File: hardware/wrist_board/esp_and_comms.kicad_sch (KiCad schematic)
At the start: 0 parts

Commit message: Added flex sensor circuitry and ESP
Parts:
- added C5, C6, C7, C8, C9: 0.1uF, symbol Device:C_Small_US
- added R10, R11, R7, R8, R9: 22k, symbol Device:R_Small
- added R6: 10k, symbol Device:R_Small
- added X1: ESP32-S3-WROOM-1-N16R8, ESP32-S3-WROOM-1-N16R8:ESP32S3WROOM1N8R2, symbol ESP32-S3-WROOM-1-N16R8:ESP32-S3-WROOM-1-N16R8
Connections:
- new net: R6.2, X1.3 (EN)
- new net +3V3: R10.2, R11.2, R6.1, R7.2, R8.2, R9.2, X1.2 (3V3)
- new net D+: X1.14 (IO20)
- new net D-: X1.13 (IO19)
- new net FS_1: C5.1, R7.1, X1.4 (IO4)
- new net FS_2: C6.1, R8.1, X1.5 (IO5)
- new net FS_3: C7.1, R9.1, X1.6 (IO6)
- new net FS_4: C8.1, R10.1, X1.7 (IO7)
- new net FS_5: C9.1, R11.1, X1.12 (IO8)
- new net GND: C5.2, C6.2, C7.2, C8.2, C9.2, X1.1 (GND), X1.40 (GND), X1.41 (GND), X1.42 (GND), X1.43 (GND), X1.44 (GND), X1.45 (GND), X1.46 (GND), X1.47 (GND), X1.48 (GND), X1.49 (GND)

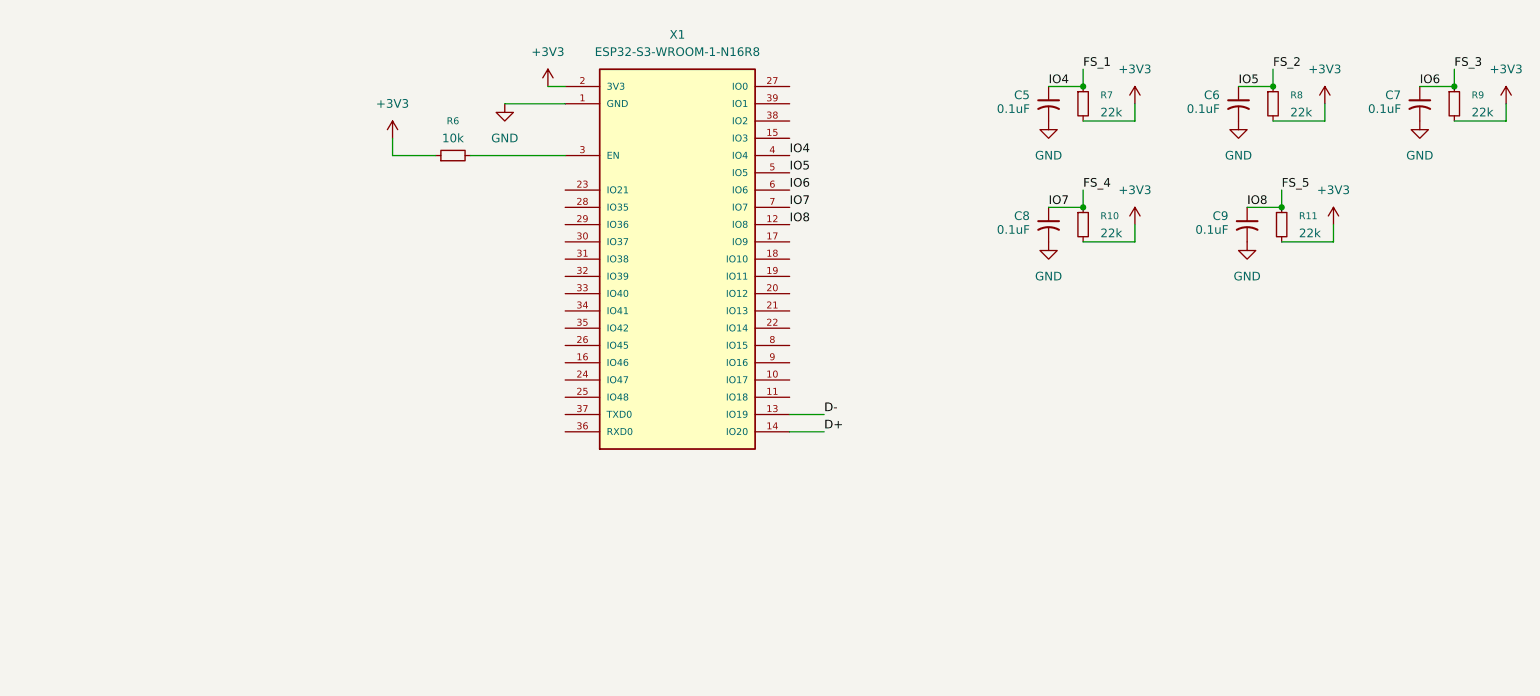
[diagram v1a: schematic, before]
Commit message: MPU 6050 IMU circuitry added
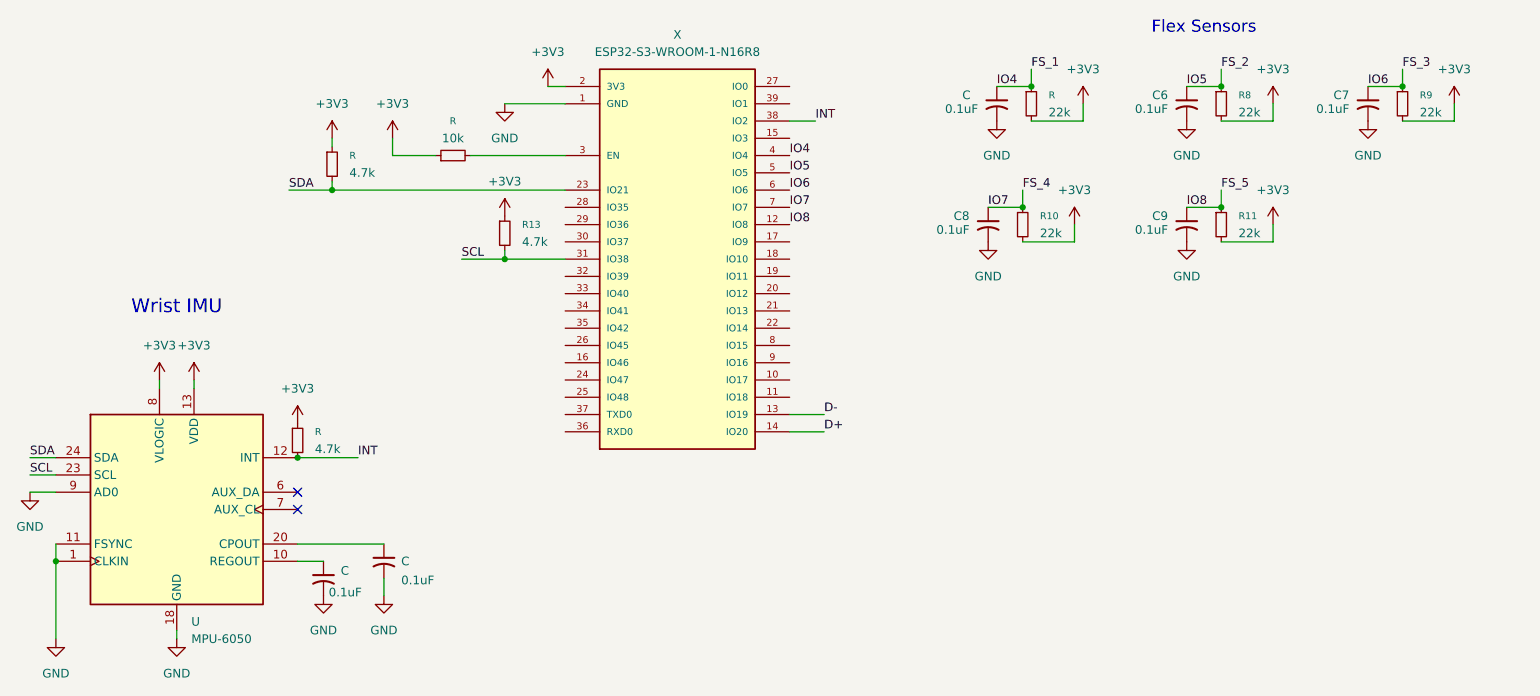
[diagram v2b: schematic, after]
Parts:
- added C (x2): 0.1uF, symbol Device:C_Small_US
- added R (x2), R13: 4.7k, symbol Device:R_Small
- added U: MPU-6050, Sensor_Motion:InvenSense_QFN-24_4x4mm_P0.5mm, symbol Sensor_Motion:MPU-6050
- renumbered C5 to C, R7 to R, R6 to R, X1 to X
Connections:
- net +3V3: now also R.1, R.1, R13.1, U.13 (VDD), U.8 (VLOGIC)
- net GND: now also C.2, C.2, U.1 (CLKIN), U.11 (FSYNC), U.18 (GND), U.9 (AD0)
- net SDA: now reaches X.23 (IO21)
- net SDA: now also R.2, U.24 (SDA)
- net SCL: now reaches X.31 (IO38)
- net SCL: now also R13.2, U.23 (SCL)
- net INT: now reaches X.38 (IO2)
- net INT: now also R.2, U.12 (INT)
- new net: C.1, U.10 (REGOUT)
- new net: C.1, U.20 (CPOUT)
- no-connect marks 0 -> 2
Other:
- note added: "Flex Sensors"
- note added: "Wrist IMU"
- moved on the sheet: C, C6, C7, C8, C9, R, R10, R11, R8, R9

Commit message: Added LEDs and power switch to power schematic
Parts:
- renumbered C to C10, C to C11, C to C5, R to R12, R to R14, R to R6, R to R7, U to U3, X to X1
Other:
- note removed: "Wrist IMU"
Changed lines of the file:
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@@
 		)
 	)
-	(text "Wrist IMU\n"
-		(exclude_from_sim no)
-		(at 69.85 108.712 0)
-		(effects
-			(font
-				(size 2.032 2.032)
-			)
-		)
-	)
 	(junction
 		(at 223.52 76.2)
@@
 		(on_board yes)
 		(dnp no)
-		(property "Reference" "C"
+		(property "Reference" "C5"
 			(at 185.42 77.47 0)
 			(effects
@@
 		(pin "1"
 		)
-		(instances)
 	)
 	(symbol
@@
 		(dnp no)
 		(fields_autoplaced yes)
-		(property "Reference" "X"
+		(property "Reference" "X1"
 			(at 143.51 68.58 0)
 			(effects
@@
 		(pin "14"
 		)
-		(instances)
 	)
 	(symbol
@@
 		(dnp no)
 		(fields_autoplaced yes)
-		(property "Reference" "U"
+		(property "Reference" "U3"
 			(at 71.9933 154.94 0)
 			(effects
@@
 		(pin "10"
 		)
-		(instances)
 	)
 	(symbol
@@
 		(dnp no)
 		(fields_autoplaced yes)
-		(property "Reference" "#PWR"
+		(property "Reference" "#PWR031"
 			(at 92.71 87.63 0)
 			(effects
@@
 		(pin "1"
 		)
-		(instances)
 	)
 	(symbol
@@
 		(dnp no)
 		(fields_autoplaced yes)
-		(property "Reference" "R"
+		(property "Reference" "R7"
 			(at 198.12 77.4699 0)
 			(effects
@@
 		(pin "1"
 		)
-		(instances)
 	)
 	(symbol
@@
 		(dnp no)
 		(fields_autoplaced yes)
-		(property "Reference" "R"
+		(property "Reference" "R14"
 			(at 90.17 126.9999 0)
 			(effects
@@
 		(pin "1"
 		)
-		(instances)
 	)
 	(symbol
@@
 		(on_board yes)
 		(dnp no)
-		(property "Reference" "C"
+		(property "Reference" "C11"
 			(at 102.87 146.05 0)
 			(effects
@@
 		(pin "1"
 		)
-		(instances)
 	)
 	(symbol
@@
 		(dnp no)
 		(fields_autoplaced yes)
-		(property "Reference" "#PWR"
+		(property "Reference" "#PWR016"
 			(at 203.2 82.55 0)
 			(effects
@@
 		(pin "1"
 		)
-		(instances)
 	)
 	(symbol
@@
 		(dnp no)
 		(fields_autoplaced yes)
-		(property "Reference" "R"
+		(property "Reference" "R6"
 			(at 110.49 81.28 90)
 			(effects
@@
 		(pin "2"
 		)
-		(instances)
 	)
 	(symbol
@@
 		(dnp no)
 		(fields_autoplaced yes)
-		(property "Reference" "#PWR"
+		(property "Reference" "#PWR013"
 			(at 124.46 80.01 0)
 			(effects
@@
 		(pin "1"
 		)
-		(instances)
 	)
 	(symbol
@@
 		(dnp no)
 		(fields_autoplaced yes)
-		(property "Reference" "#PWR"
+		(property "Reference" "#PWR028"
 			(at 69.85 163.83 0)
 			(effects
@@
 		(pin "1"
 		)
-		(instances)
 	)
 	(symbol
@@
 		(dnp no)
 		(fields_autoplaced yes)
-		(property "Reference" "#PWR"
+		(property "Reference" "#PWR034"
 			(at 87.63 129.54 0)
 			(effects
@@
 		(pin "1"
 		)
-		(instances)
 	)
 	(symbol
@@
 		(dnp no)
 		(fields_autoplaced yes)
-		(property "Reference" "R"
+		(property "Reference" "R12"
 			(at 95.25 86.3599 0)
 			(effects
@@
 		(pin "1"
 		)
-		(instances)
 	)
 	(symbol
@@
 		(dnp no)
 		(fields_autoplaced yes)
-		(property "Reference" "#PWR"
+		(property "Reference" "#PWR033"
 			(at 48.26 142.24 0)
 			(effects
@@
 		(pin "1"
 		)
-		(instances)
 	)
 	(symbol
@@
 		(dnp no)
 		(fields_autoplaced yes)
-		(property "Reference" "#PWR"
+		(property "Reference" "#PWR014"
 			(at 118.11 85.09 0)
 			(effects
@@
 		(pin "1"
 		)
-		(instances)
 	)
 	(symbol
@@
 		(dnp no)
 		(fields_autoplaced yes)
-		(property "Reference" "#PWR"
+		(property "Reference" "#PWR027"
 			(at 67.31 123.19 0)
 			(effects
@@
 		(pin "1"
 		)
-		(instances)
 	)
 	(symbol
@@
 		(dnp no)
 		(fields_autoplaced yes)
-		(property "Reference" "#PWR"
+		(property "Reference" "#PWR030"
 			(at 100.33 157.48 0)
 			(effects
@@
 		(pin "1"
 		)
-		(instances)
 	)
 	(symbol
@@
 		(dnp no)
 		(fields_autoplaced yes)
-		(property "Reference" "#PWR"
+		(property "Reference" "#PWR029"
 			(at 91.44 157.48 0)
 			(effects
@@
 		(pin "1"
 		)
-		(instances)
 	)
 	(symbol
@@
 		(dnp no)
 		(fields_autoplaced yes)
-		(property "Reference" "#PWR"
+		(property "Reference" "#PWR015"
 			(at 101.6 87.63 0)
 			(effects
@@
 		(pin "1"
 		)
-		(instances)
 	)
 	(symbol
@@
 		(dnp no)
 		(fields_autoplaced yes)
-		(property "Reference" "#PWR"
+		(property "Reference" "#PWR026"
 			(at 72.39 123.19 0)
 			(effects
@@
 		(pin "1"
 		)
-		(instances)
 	)
 	(symbol
@@
 		(dnp no)
 		(fields_autoplaced yes)
-		(property "Reference" "#PWR"
+		(property "Reference" "#PWR017"
 			(at 190.5 87.63 0)
 			(effects
@@
 		(pin "1"
 		)
-		(instances)
 	)
 	(symbol
@@
 		(on_board yes)
 		(dnp no)
-		(property "Reference" "C"
+		(property "Reference" "C10"
 			(at 93.98 147.4469 0)
 			(effects
@@
 		(pin "1"
 		)
-		(instances)
 	)
 	(symbol

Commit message: USB C 2.0 receptacle updated
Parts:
- renumbered C5 to C?, C11 to C?, C10 to C?, R7 to R?, R14 to R?, R6 to R?, R12 to R?, U3 to U?, X1 to X?
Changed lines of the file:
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@@
 		(on_board yes)
 		(dnp no)
-		(property "Reference" "C5"
+		(property "Reference" "C?"
 			(at 185.42 77.47 0)
 			(effects
@@
 		(pin "1"
 		)
+		(instances
+			(project "wrist_board"
+				(path "/530b8e3e-eee5-4922-ab86-607fb3fa4192/d316cad0-6949-4839-9637-d12d2d6e31b9"
+					(reference "C?")
+					(unit 1)
+				)
+			)
+		)
 	)
 	(symbol
@@
 		(dnp no)
 		(fields_autoplaced yes)
-		(property "Reference" "X1"
+		(property "Reference" "X?"
 			(at 143.51 68.58 0)
 			(effects
@@
 		(pin "14"
 		)
+		(instances
+			(project "wrist_board"
+				(path "/530b8e3e-eee5-4922-ab86-607fb3fa4192/d316cad0-6949-4839-9637-d12d2d6e31b9"
+					(reference "X?")
+					(unit 1)
+				)
+			)
+		)
 	)
 	(symbol
@@
 		(dnp no)
 		(fields_autoplaced yes)
-		(property "Reference" "U3"
+		(property "Reference" "U?"
 			(at 71.9933 154.94 0)
 			(effects
@@
 		(pin "10"
 		)
+		(instances
+			(project "wrist_board"
+				(path "/530b8e3e-eee5-4922-ab86-607fb3fa4192/d316cad0-6949-4839-9637-d12d2d6e31b9"
+					(reference "U?")
+					(unit 1)
+				)
+			)
+		)
 	)
 	(symbol
@@
 		(dnp no)
 		(fields_autoplaced yes)
-		(property "Reference" "#PWR031"
+		(property "Reference" "#PWR?"
 			(at 92.71 87.63 0)
 			(effects
@@
 		(pin "1"
 		)
+		(instances
+			(project "wrist_board"
+				(path "/530b8e3e-eee5-4922-ab86-607fb3fa4192/d316cad0-6949-4839-9637-d12d2d6e31b9"
+					(reference "#PWR?")
+					(unit 1)
+				)
+			)
+		)
 	)
 	(symbol
@@
 		(dnp no)
 		(fields_autoplaced yes)
-		(property "Reference" "R7"
+		(property "Reference" "R?"
 			(at 198.12 77.4699 0)
 			(effects
@@
 		(pin "1"
 		)
+		(instances
+			(project "wrist_board"
+				(path "/530b8e3e-eee5-4922-ab86-607fb3fa4192/d316cad0-6949-4839-9637-d12d2d6e31b9"
+					(reference "R?")
+					(unit 1)
+				)
+			)
+		)
 	)
 	(symbol
@@
 		(dnp no)
 		(fields_autoplaced yes)
-		(property "Reference" "R14"
+		(property "Reference" "R?"
 			(at 90.17 126.9999 0)
 			(effects
@@
 		(pin "1"
 		)
+		(instances
+			(project "wrist_board"
+				(path "/530b8e3e-eee5-4922-ab86-607fb3fa4192/d316cad0-6949-4839-9637-d12d2d6e31b9"
+					(reference "R?")
+					(unit 1)
+				)
+			)
+		)
 	)
 	(symbol
@@
 		(on_board yes)
 		(dnp no)
-		(property "Reference" "C11"
+		(property "Reference" "C?"
 			(at 102.87 146.05 0)
 			(effects
@@
 		(pin "1"
 		)
+		(instances
+			(project "wrist_board"
+				(path "/530b8e3e-eee5-4922-ab86-607fb3fa4192/d316cad0-6949-4839-9637-d12d2d6e31b9"
+					(reference "C?")
+					(unit 1)
+				)
+			)
+		)
 	)
 	(symbol
@@
 		(dnp no)
 		(fields_autoplaced yes)
-		(property "Reference" "#PWR016"
+		(property "Reference" "#PWR?"
 			(at 203.2 82.55 0)
 			(effects
@@
 		(pin "1"
 		)
+		(instances
+			(project "wrist_board"
+				(path "/530b8e3e-eee5-4922-ab86-607fb3fa4192/d316cad0-6949-4839-9637-d12d2d6e31b9"
+					(reference "#PWR?")
+					(unit 1)
+				)
+			)
+		)
 	)
 	(symbol
@@
 		(dnp no)
 		(fields_autoplaced yes)
-		(property "Reference" "R6"
+		(property "Reference" "R?"
 			(at 110.49 81.28 90)
 			(effects
@@
 		(pin "2"
 		)
+		(instances
+			(project "wrist_board"
+				(path "/530b8e3e-eee5-4922-ab86-607fb3fa4192/d316cad0-6949-4839-9637-d12d2d6e31b9"
+					(reference "R?")
+					(unit 1)
+				)
+			)
+		)
 	)
 	(symbol
@@
 		(dnp no)
 		(fields_autoplaced yes)
-		(property "Reference" "#PWR013"
+		(property "Reference" "#PWR?"
 			(at 124.46 80.01 0)
 			(effects
@@
 		(pin "1"
 		)
+		(instances
+			(project "wrist_board"
+				(path "/530b8e3e-eee5-4922-ab86-607fb3fa4192/d316cad0-6949-4839-9637-d12d2d6e31b9"
+					(reference "#PWR?")
+					(unit 1)
+				)
+			)
+		)
 	)
 	(symbol
@@
 		(dnp no)
 		(fields_autoplaced yes)
-		(property "Reference" "#PWR028"
+		(property "Reference" "#PWR?"
 			(at 69.85 163.83 0)
 			(effects
@@
 		(pin "1"
 		)
+		(instances
+			(project "wrist_board"
+				(path "/530b8e3e-eee5-4922-ab86-607fb3fa4192/d316cad0-6949-4839-9637-d12d2d6e31b9"
+					(reference "#PWR?")
+					(unit 1)
+				)
+			)
+		)
 	)
 	(symbol
@@
 		(dnp no)
 		(fields_autoplaced yes)
-		(property "Reference" "#PWR034"
+		(property "Reference" "#PWR?"
 			(at 87.63 129.54 0)
 			(effects
@@
 		(pin "1"
 		)
+		(instances
+			(project "wrist_board"
+				(path "/530b8e3e-eee5-4922-ab86-607fb3fa4192/d316cad0-6949-4839-9637-d12d2d6e31b9"
+					(reference "#PWR?")
+					(unit 1)
+				)
+			)
+		)
 	)
 	(symbol
@@
 		(dnp no)
 		(fields_autoplaced yes)
-		(property "Reference" "R12"
+		(property "Reference" "R?"
 			(at 95.25 86.3599 0)
 			(effects
@@
 		(pin "1"
 		)
+		(instances
+			(project "wrist_board"
+				(path "/530b8e3e-eee5-4922-ab86-607fb3fa4192/d316cad0-6949-4839-9637-d12d2d6e31b9"
+					(reference "R?")
+					(unit 1)
+				)
+			)
+		)
 	)
 	(symbol
@@
 		(dnp no)
 		(fields_autoplaced yes)
-		(property "Reference" "#PWR033"
+		(property "Reference" "#PWR?"
 			(at 48.26 142.24 0)
 			(effects
@@
 		(pin "1"
 		)
+		(instances
+			(project "wrist_board"
+				(path "/530b8e3e-eee5-4922-ab86-607fb3fa4192/d316cad0-6949-4839-9637-d12d2d6e31b9"
+					(reference "#PWR?")
+					(unit 1)
+				)
+			)
+		)
 	)
 	(symbol
@@
 		(dnp no)
 		(fields_autoplaced yes)
-		(property "Reference" "#PWR014"
+		(property "Reference" "#PWR?"
 			(at 118.11 85.09 0)
 			(effects
@@
 		(pin "1"
 		)
+		(instances
+			(project "wrist_board"
+				(path "/530b8e3e-eee5-4922-ab86-607fb3fa4192/d316cad0-6949-4839-9637-d12d2d6e31b9"
+					(reference "#PWR?")
+					(unit 1)
+				)
+			)
+		)
 	)
 	(symbol
@@
 		(dnp no)
 		(fields_autoplaced yes)
-		(property "Reference" "#PWR027"
+		(property "Reference" "#PWR?"
 			(at 67.31 123.19 0)
 			(effects
@@
 		(pin "1"
 		)
+		(instances
+			(project "wrist_board"
+				(path "/530b8e3e-eee5-4922-ab86-607fb3fa4192/d316cad0-6949-4839-9637-d12d2d6e31b9"
+					(reference "#PWR?")
+					(unit 1)
+				)
+			)
+		)
 	)
 	(symbol
@@
 		(dnp no)
 		(fields_autoplaced yes)
-		(property "Reference" "#PWR030"
+		(property "Reference" "#PWR?"
 			(at 100.33 157.48 0)
 			(effects
@@
 		(pin "1"
 		)
+		(instances
+			(project "wrist_board"
+				(path "/530b8e3e-eee5-4922-ab86-607fb3fa4192/d316cad0-6949-4839-9637-d12d2d6e31b9"
+					(reference "#PWR?")
+					(unit 1)
+				)
+			)
+		)
 	)
 	(symbol
@@
 		(dnp no)
 		(fields_autoplaced yes)
-		(property "Reference" "#PWR029"
+		(property "Reference" "#PWR?"
 			(at 91.44 157.48 0)
 			(effects
@@
 		(pin "1"
 		)
+		(instances
+			(project "wrist_board"
+				(path "/530b8e3e-eee5-4922-ab86-607fb3fa4192/d316cad0-6949-4839-9637-d12d2d6e31b9"
+					(reference "#PWR?")
+					(unit 1)
+				)
+			)
+		)
 	)
 	(symbol
@@
 		(dnp no)
 		(fields_autoplaced yes)
-		(property "Reference" "#PWR015"
+		(property "Reference" "#PWR?"
 			(at 101.6 87.63 0)
 			(effects
@@
 		(pin "1"
 		)
+		(instances
+			(project "wrist_board"
+				(path "/530b8e3e-eee5-4922-ab86-607fb3fa4192/d316cad0-6949-4839-9637-d12d2d6e31b9"
+					(reference "#PWR?")
+					(unit 1)
+				)
+			)
+		)
 	)
 	(symbol
@@
 		(dnp no)
 		(fields_autoplaced yes)
-		(property "Reference" "#PWR026"
+		(property "Reference" "#PWR?"
 			(at 72.39 123.19 0)
 			(effects
@@
 		(pin "1"
 		)
+		(instances
+			(project "wrist_board"
+				(path "/530b8e3e-eee5-4922-ab86-607fb3fa4192/d316cad0-6949-4839-9637-d12d2d6e31b9"
+					(reference "#PWR?")
+					(unit 1)
+				)
+			)
+		)
 	)
 	(symbol
@@
 		(dnp no)
 		(fields_autoplaced yes)
-		(property "Reference" "#PWR017"
+		(property "Reference" "#PWR?"
 			(at 190.5 87.63 0)
 			(effects
@@
 		(pin "1"
 		)
+		(instances
+			(project "wrist_board"
+				(path "/530b8e3e-eee5-4922-ab86-607fb3fa4192/d316cad0-6949-4839-9637-d12d2d6e31b9"
+					(reference "#PWR?")
+					(unit 1)
+				)
+			)
+		)
 	)
 	(symbol
@@
 		(on_board yes)
 		(dnp no)
-		(property "Reference" "C10"
+		(property "Reference" "C?"
 			(at 93.98 147.4469 0)
 			(effects
@@
 		(pin "1"
 		)
-	)
+		(instances
+			(project "wrist_board"
+				(path "/530b8e3e-eee5-4922-ab86-607fb3fa4192/d316cad0-6949-4839-9637-d12d2d6e31b9"
+					(reference "C?")
+					(unit 1)
+				)
+			)
+		)
+	)

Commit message: Added male 2.54mm headers for flex sensor connection
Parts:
- added J3, J4, J5, J6, J7: Conn_01x02, symbol Connector_Generic:Conn_01x02
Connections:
- net FS_1: now also J3.1 (Pin_1)
- net FS_2: now also J4.1 (Pin_1)
- net FS_3: now also J5.1 (Pin_1)
- net FS_4: now also J6.1 (Pin_1)
- net FS_5: now also J7.1 (Pin_1)
- net GND: now also J3.2 (Pin_2), J4.2 (Pin_2), J5.2 (Pin_2), J6.2 (Pin_2), J7.2 (Pin_2)

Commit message: Minor updates to both power and esp schematics
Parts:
- added C5: 0.1uF, symbol Device:C_Small_US
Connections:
- net +3V3: now also C5.1
- net GND: now also C5.2
- no-connect marks 2 -> 27

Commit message: All prototype footprints assigned
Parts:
- C11, C12, C13: renamed from C?; footprint (none) -> Capacitor_SMD:C_0402_1005Metric
- C5, C6, C7, C8, C9: footprint (none) -> Capacitor_SMD:C_0402_1005Metric
- J3, J4, J5, J6, J7: footprint (none) -> Connector_PinHeader_2.54mm:PinHeader_1x02_P2.54mm_Vertical
- R10, R11, R13, R8, R9: footprint (none) -> Resistor_SMD:R_0402_1005Metric
- R12, R14, R6, R7: renamed from R?; footprint (none) -> Resistor_SMD:R_0402_1005Metric
- gave numbers to parts that had none: 2

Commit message: Schematics condensed into one, labels added
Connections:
- no-connect marks 27 -> 28
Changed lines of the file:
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@@
+	)
+	(no_connect
+		(at 160.02 83.82)
 	)
 	(no_connect
@@
 		)
 	)
-	(label "D+"
-		(at 165.1 127 0)
-		(effects
-			(font
-				(size 1.27 1.27)
-			)
-			(justify left bottom)
-		)
-	)
 	(label "SCL"
 		(at 48.26 133.35 0)
@@
 		)
 	)
-	(label "D-"
-		(at 165.1 124.46 0)
-		(effects
-			(font
-				(size 1.27 1.27)
-			)
-			(justify left bottom)
-		)
-	)
 	(label "FS_3"
 		(at 250.19 73.66 0)
@@
 		)
 	)
+	(hierarchical_label "D+"
+		(shape bidirectional)
+		(at 165.1 127 0)
+		(effects
+			(font
+				(size 1.27 1.27)
+			)
+			(justify left)
+		)
+	)
+	(hierarchical_label "D-"
+		(shape bidirectional)
+		(at 165.1 124.46 0)
+		(effects
+			(font
+				(size 1.27 1.27)
+			)
+			(justify left)
+		)
+	)
